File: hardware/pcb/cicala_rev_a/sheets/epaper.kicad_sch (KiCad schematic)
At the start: 23 parts, among them J2 FH12-24S-0.5SH, Q1 Si1308EDL, U6 TPS22917DBVR

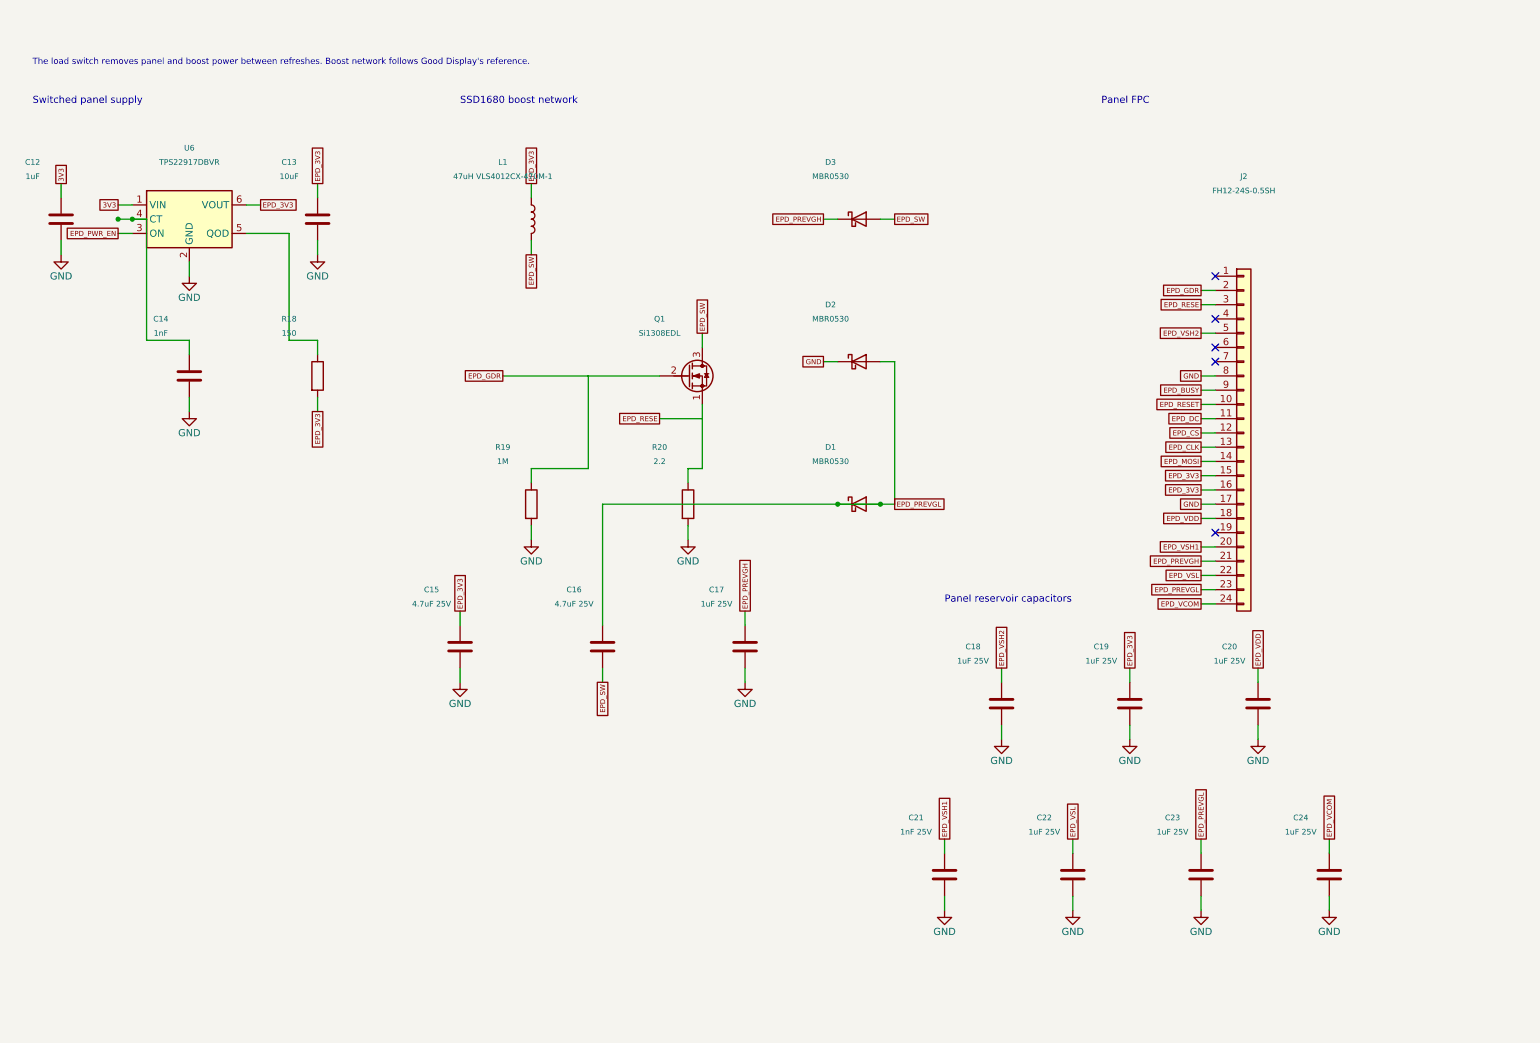
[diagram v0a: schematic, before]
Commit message: fix(hw): split the shorted USB pair and PREVGL pump node
Sheet re-layout that also separates two nets that were tied together.

J1 CC2, D+ and D- shared one net with both USBLC6 line pins; D+ and D-
are now their own nets. D1 had both pins on EPD_PREVGL, shorting it out
of the charge pump; its cathode is now the pump node with C16.

Three net labels were lost in the move and are now auto-named:
BATT_NTC, BTN_CATEGORY and BTN_NEXT. pin_contract.csv and BOM.md still
name them, so they need restoring.

Co-Authored-By: Claude Opus 5 (1M context) <noreply@anthropic.com>
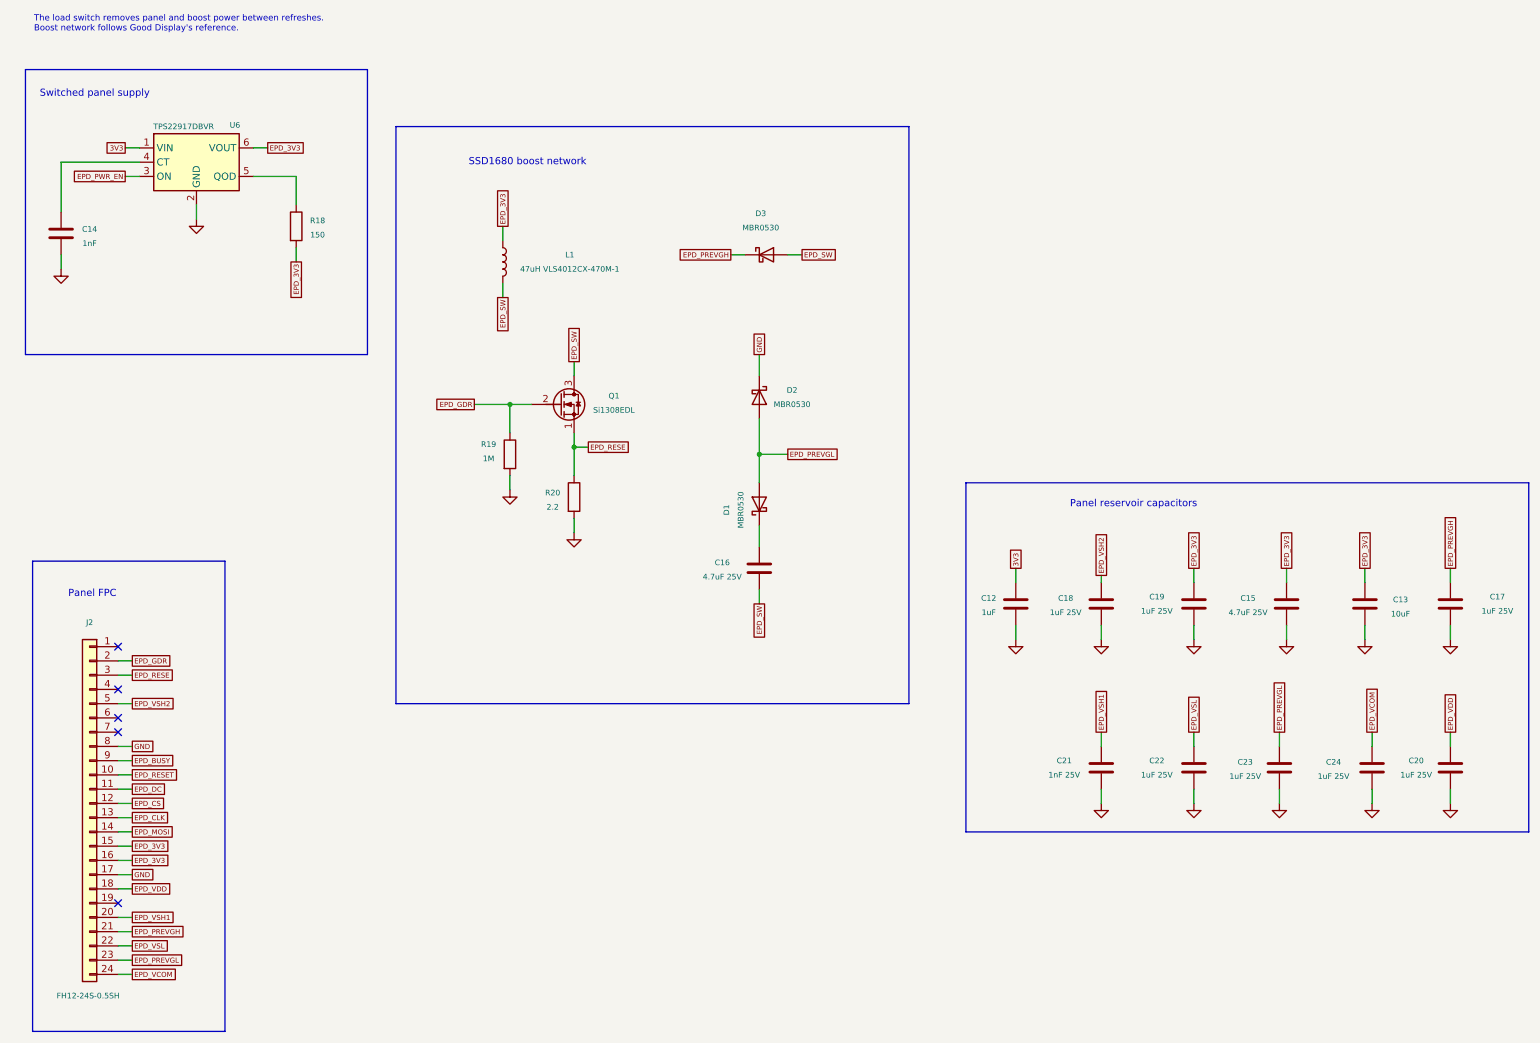
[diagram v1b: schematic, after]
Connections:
- net EPD_PREVGL: no longer C16.1, D1.1 (K)
- new net: C16.1, D1.1 (K)
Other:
- moved on the sheet: C12, C13, C14, C15, C16, C17, C18, C19, C20, C21, C22, C23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

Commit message: fix(hw): correct four ERC-invisible rev A wiring errors
All four are electrically valid connections that are simply wrong, which
is why ERC accepted them. Verified against the part datasheets and the
GDEY0213B74 reference circuit, and checked by re-exporting the netlist.

USB D+/D- were crossed between the receptacle and the MCU: J1 D- reached
GPIO20 (USB_D+) through U4 I/O1 and R3. Swapping the USB_DP and USB_DN
labels puts each line on its own pin without crossing wires. R3 now
carries D-, R4 carries D+.

Q1 used Q_NMOS_SGD, but the Si1308EDL in SOT-323 is pin 1 = G, 2 = S,
3 = D, so the gate driver landed on the sense node. The symbol is now
Q_NMOS_GSD; the drawing is unchanged because both symbols share the same
pin geometry.

D2's anode sat on EPD_PREVGL rather than on the pump node, leaving C16
with no charging path, so the negative rail could never develop. D1's
cathode, D2's anode and C16 now meet on EPD_PUMP, with D1 branching off
to EPD_PREVGL, as in the panel reference circuit.

C21 was 1 nF on VSH1, a driving rail the reference gives 1 uF/25 V.

Also restores three net names lost in the sheet re-layout: BATT_NTC,
BTN_CATEGORY and BTN_NEXT.

Co-Authored-By: Claude Opus 5 (1M context) <noreply@anthropic.com>
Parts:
- C21: value 1nF 25V -> 1uF 25V
- Q1: symbol Transistor_FET:Q_NMOS_SGD -> Transistor_FET:Q_NMOS_GSD
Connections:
- net EPD_GDR: now also Q1.1 (G); no longer Q1.2 (G)
- net EPD_PREVGL: no longer D2.2 (A)
- net EPD_RESE: now also Q1.2 (S); no longer Q1.1 (S)
- net EPD_PUMP: now reaches C16.1, D1.1 (K)
- net EPD_PUMP: now also D2.2 (A)
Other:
- moved on the sheet: D1
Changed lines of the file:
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@@
 	(wire
 		(pts
-			(xy 190.5 115.57) (xy 190.5 113.03)
+			(xy 144.78 92.71) (xy 144.78 109.22)
 		)
 		(stroke
@@
 	(wire
 		(pts
-			(xy 144.78 92.71) (xy 144.78 97.79)
+			(xy 144.78 92.71) (xy 148.59 92.71)
+		)
+		(stroke
+			(width 0)
+			(type default)
+		)
+	)
+	(wire
+		(pts
+			(xy 156.21 92.71) (xy 163.83 92.71)
+		)
+		(stroke
+			(width 0)
+			(type default)
+		)
+	)
+	(wire
+		(pts
+			(xy 190.5 115.57) (xy 190.5 113.03)
 		)
 		(stroke
@@
 	(wire
 		(pts
-			(xy 144.78 105.41) (xy 144.78 109.22)
-		)
-		(stroke
-			(width 0)
-			(type default)
-		)
-	)
-	(wire
-		(pts
 			(xy 149.86 57.15) (xy 152.4 57.15)
 		)
@@
 	(wire
 		(pts
-			(xy 144.78 92.71) (xy 149.86 92.71)
+			(xy 62.23 55.88) (xy 62.23 58.42)
 		)
 		(stroke
@@
 		)
 	)
-	(wire
-		(pts
-			(xy 62.23 55.88) (xy 62.23 58.42)
+	(global_label "EPD_PUMP"
+		(shape passive)
+		(at 144.78 104.14 0)
+		(fields_autoplaced yes)
+		(effects
+			(font
+				(size 0.9 0.9)
+			)
+			(justify left)
 		)
-		(stroke
-			(width 0)
-			(type default)
+		(property "Intersheetrefs" "${INTERSHEET_REFS}"
+			(at 144.78 104.14 0)
+			(hide yes)
+			(show_name no)
+			(do_not_autoplace no)
+			(effects
+				(font
+					(size 0.8 0.8)
+				)
+			)
 		)
 	)
@@
 	(global_label "EPD_PREVGL"
 		(shape passive)
-		(at 149.86 92.71 0)
+		(at 163.83 92.71 0)
 		(fields_autoplaced yes)
 		(effects
@@
 		)
 		(property "Intersheetrefs" "${INTERSHEET_REFS}"
-			(at 149.86 92.71 0)
+			(at 163.83 92.71 0)
 			(hide yes)
 			(show_name no)
@@
 	)
 	(symbol
-		(lib_id "Transistor_FET:Q_NMOS_SGD")
+		(lib_id "Transistor_FET:Q_NMOS_GSD")
 		(at 109.22 83.82 0)
 		(unit 1)
@@
 			)
 		)
-		(property "Value" "1nF 25V"
+		(property "Value" "1uF 25V"
 			(at 199.136 149.86 0)
 			(show_name no)
@@
 	(symbol
 		(lib_id "Device:D_Schottky")
-		(at 144.78 101.6 90)
+		(at 152.4 92.71 0)
 		(unit 1)
 		(body_style 1)
@@
 		(dnp no)
 		(property "Reference" "D1"
-			(at 138.938 102.616 0)
+			(at 152.4 96.52 0)
 			(show_name no)
 			(do_not_autoplace no)
@@
 		)
 		(property "Value" "MBR0530"
-			(at 141.478 102.616 0)
+			(at 152.4 99.06 0)
 			(show_name no)
 			(do_not_autoplace no)
@@
 		)
 		(property "Footprint" "Diode_SMD:D_SOD-123"
-			(at 144.78 101.6 0)
+			(at 152.4 92.71 0)
 			(hide yes)
 			(show_name no)
@@
 		)
 		(property "Datasheet" "~"
-			(at 144.78 101.6 0)
+			(at 152.4 92.71 0)
 			(hide yes)
 			(show_name no)
@@
 		)
 		(property "Description" "Schottky diode"
-			(at 144.78 101.6 0)
+			(at 152.4 92.71 0)
 			(hide yes)
 			(show_name no)
@@
 		)
 		(property "MPN" "MBR0530"
-			(at 144.78 101.6 0)
+			(at 152.4 92.71 0)
 			(hide yes)
 			(show_name no)

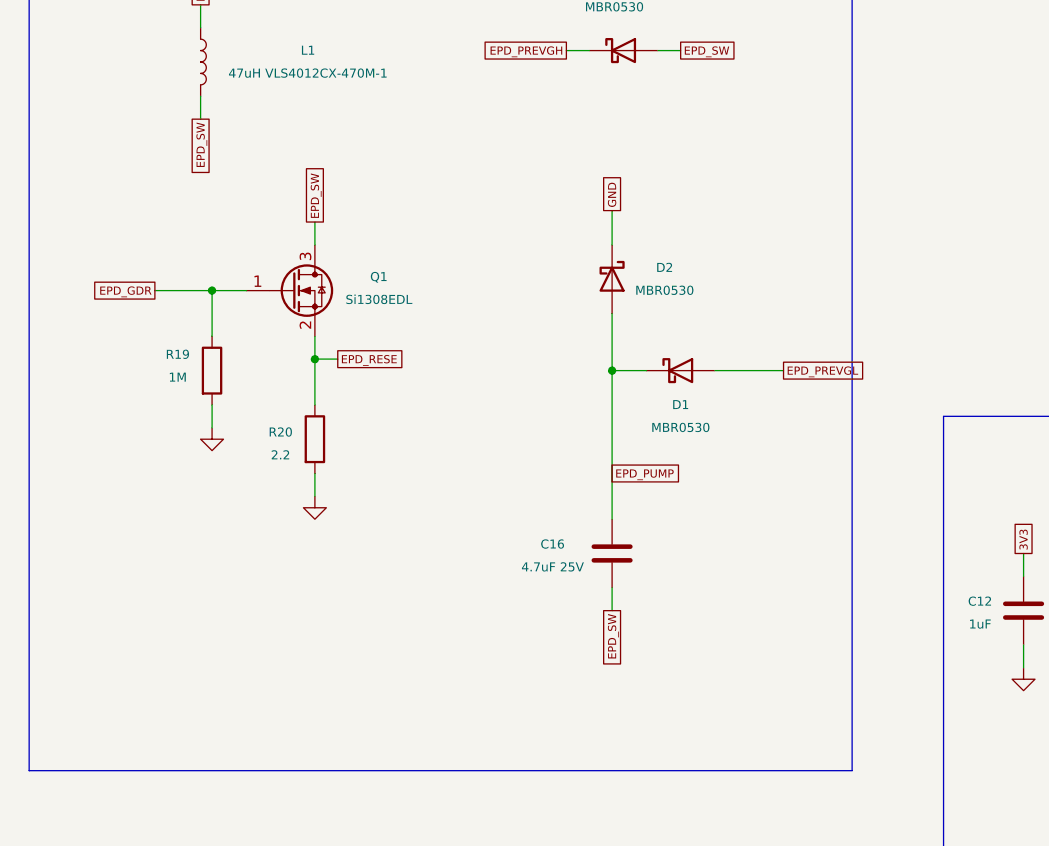
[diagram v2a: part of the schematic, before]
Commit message: style(hw): tidy the rev A sheet layout
Component and label placement only. The exported netlist and BOM are
identical to the previous commit, and ERC, DRC and STEP export pass.

Co-Authored-By: Claude Opus 5 (1M context) <noreply@anthropic.com>
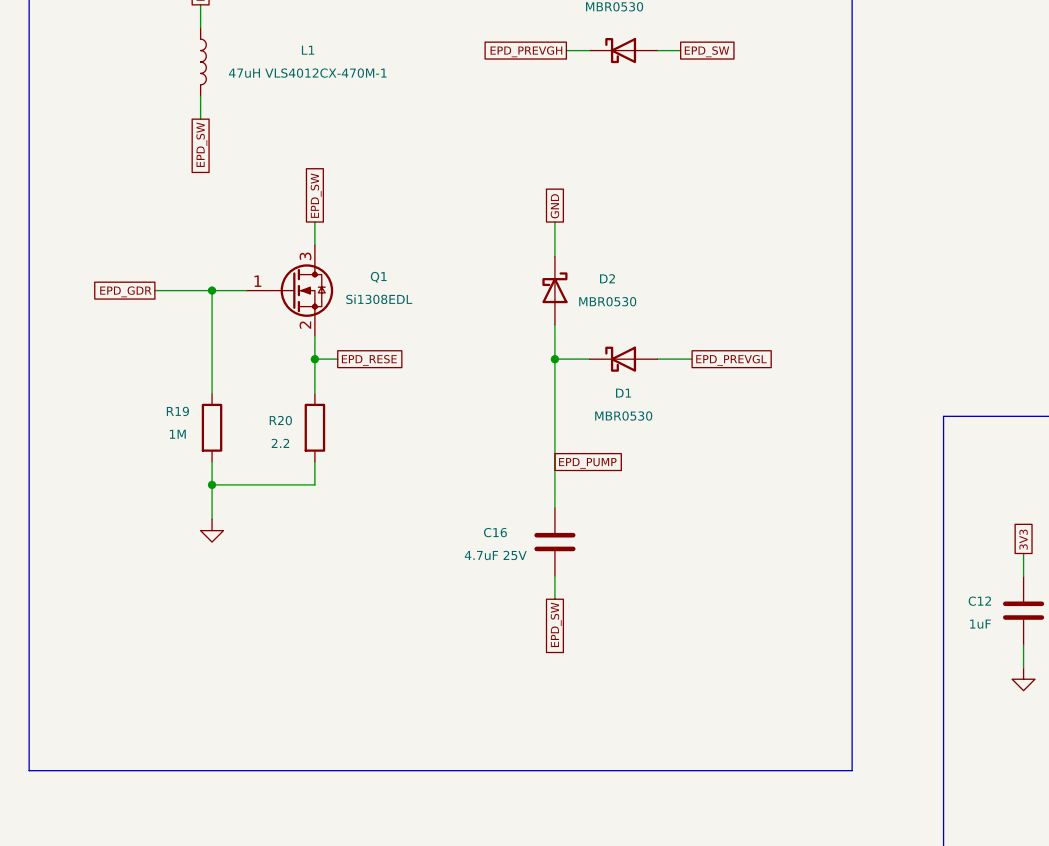
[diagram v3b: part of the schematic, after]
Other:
- moved on the sheet: C16, D1, D2, R19, R20

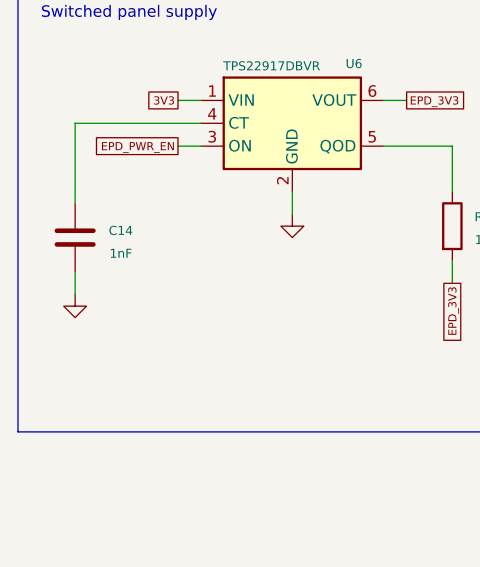
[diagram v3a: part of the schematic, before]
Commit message: fix(hw): correct the VBUS divider and the TPS22917 slew capacitor
R5 and R6 were the wrong way round: 150 k from VBUS to the sense node over
100 k to ground gives 2.0 V from a 5 V bus, below the ESP32-S3 guaranteed
high-input threshold at 3.3 V. Swapping them gives 3.0 V, which is what the
DevKitC overlay already assumes.

C14 returned to GND. The TPS22917 slew capacitor is referenced to VIN, not
GND (SLVSDW8B section 9.3.2, "A capacitor to VIN on the CT pin sets the slew
rate of VOUT"), so its far side moves to the U6 3V3 input rail.

Neither error was visible to ERC; both are electrically valid connections
that compute the wrong answer.

Co-Authored-By: Claude Opus 5 <noreply@anthropic.com>
Claude-Session: https://claude.ai/code/session_01E5vy1HJsPztSk9nFw6j5Ko
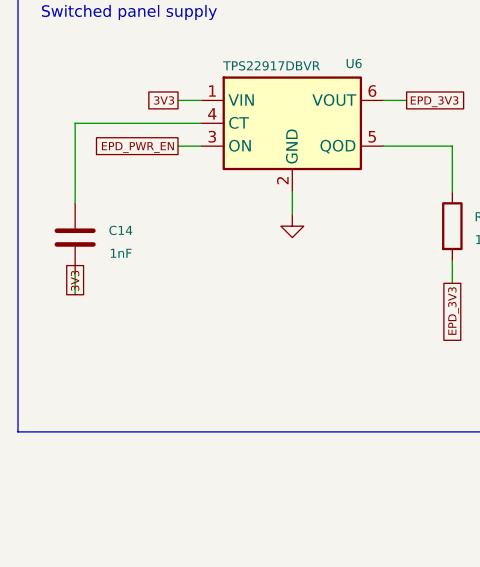
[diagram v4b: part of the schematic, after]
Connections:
- net 3V3: now also C14.2
- net GND: no longer C14.2
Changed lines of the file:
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@@
-	(symbol
-		(lib_id "power:GND")
-		(at 20.32 59.69 0)
-		(unit 1)
-		(body_style 1)
-		(exclude_from_sim no)
-		(in_bom yes)
-		(on_board yes)
-		(in_pos_files yes)
-		(dnp no)
-		(property "Reference" "#PWR0155"
-			(at 20.32 66.04 0)
-			(hide yes)
-			(show_name no)
-			(do_not_autoplace no)
-			(effects
-				(font
-					(size 1.27 1.27)
-				)
-			)
-		)
-		(property "Value" "GND"
-			(at 20.32 63.5 0)
-			(hide yes)
-			(show_name no)
-			(do_not_autoplace no)
-			(effects
-				(font
-					(size 1.27 1.27)
-				)
-			)
-		)
-		(property "Footprint" ""
-			(at 20.32 59.69 0)
-			(hide yes)
-			(show_name no)
-			(do_not_autoplace no)
-			(effects
-				(font
-					(size 1.27 1.27)
-				)
-			)
-		)
-		(property "Datasheet" ""
-			(at 20.32 59.69 0)
-			(hide yes)
-			(show_name no)
-			(do_not_autoplace no)
-			(effects
-				(font
-					(size 1.27 1.27)
-				)
-			)
-		)
-		(property "Description" "Power symbol creates a global label with name GND, ground"
-			(at 20.32 59.69 0)
-			(hide yes)
-			(show_name no)
-			(do_not_autoplace no)
-			(effects
-				(font
-					(size 1.27 1.27)
-				)
-			)
-		)
-		(pin "1"
-		)
-		(instances
-			(project "cicala_rev_a"
-				(path "/9b5e4c31-c66f-4b64-9ff8-62a2c447d0bc/9467d62a-f8ed-46c9-a7cb-f7af887ddb15"
-					(reference "#PWR0155")
-					(unit 1)
-				)
-			)
-		)
-	)
 	(symbol
 		(lib_id "power:GND")
@@
 				)
 			)
+		)
+	)
+	(global_label "3V3"
+		(shape passive)
+		(at 20.32 59.69 270)
+		(fields_autoplaced yes)
+		(effects
+			(font
+				(size 0.9 0.9)
+			)
+			(justify left)
+		)
+		(property "Intersheetrefs" "${INTERSHEET_REFS}"
+			(at 20.32 59.69 0)
+			(hide yes)
+			(show_name no)
+			(do_not_autoplace no)
+			(effects
+				(font
+					(size 0.8 0.8)
+				)
+			)
